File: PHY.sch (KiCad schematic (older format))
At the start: 70 parts

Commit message: Component placement
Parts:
- C10, C11, C12, C13, C14, C15, C16, C3, C4, C5, C6, C7, C8, C9: renamed from C?; footprint (none) -> Capacitor_SMD:C_0402_1005Metric
- D3: renamed from D?; footprint (none) -> LED_SMD:LED_0603_1608Metric
- J10: renamed from J?; footprint (none) -> Connector_RJ:RJ45_Hanrun_HR911105A
- JP1: renamed from J?; footprint (none) -> Connector_PinHeader_2.54mm:PinHeader_1x02_P2.54mm_Vertical
- JP2, JP3, JP4, JP5, JP6: renamed from J?; footprint (none) -> Connector_PinHeader_2.54mm:PinHeader_1x03_P2.54mm_Vertical
- R10, R11, R12, R13, R14, R15, R16, R17, R18, R19, R20, R21, R22, R23, R24, R25, R26, R27, R28, R29, R30, R31, R32, R33, R34, R35, R36, R37, R38, R39, R40, R41, R42, R43, R44, R45, R46, R47, R48, R49, R50, R6, R7, R8, R9: renamed from R?; footprint (none) -> Resistor_SMD:R_0402_1005Metric
- T1: renamed from T?; footprint (none) -> ak:Transformer_Pulse_H1100NL
- gave numbers to parts that had none: 2

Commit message: Test...
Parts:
- added R98, R99: 0, Resistor_SMD:R_1206_3216Metric, symbol Device:R_Small
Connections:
- net GND: now also R98.1, R99.1
- net GNDPWR: now also R98.2, R99.2
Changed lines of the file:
@@
 Text Label 9050 5900 0    50   ~ 0
 AN0
+$Comp
+L power:GNDPWR #PWR078
+U 1 1 5FE14DAE
+P 9250 3300
+F 0 "#PWR078" H 9250 3100 50  0001 C CNN
+F 1 "GNDPWR" H 9254 3146 50  0001 C CNN
+F 2 "" H 9250 3250 50  0001 C CNN
+F 3 "" H 9250 3250 50  0001 C CNN
+	1    9250 3300
+	1    0    0    -1
+$EndComp
+$Comp
+L Device:R_Small R99
+U 1 1 5FE160E3
+P 9400 3200
+F 0 "R99" V 9204 3200 50  0000 C CNN
+F 1 "0" V 9295 3200 50  0000 C CNN
+F 2 "Resistor_SMD:R_1206_3216Metric" H 9400 3200 50  0001 C CNN
+F 3 "~" H 9400 3200 50  0001 C CNN
+	1    9400 3200
+	0    1    1    0
+$EndComp
+$Comp
+L power:GND #PWR?
+U 1 1 5FE166F9
+P 9550 3300
+AR Path="/5FE166F9" Ref="#PWR?"  Part="1"
+AR Path="/6062FABA/5FE166F9" Ref="#PWR080"  Part="1"
+F 0 "#PWR080" H 9550 3050 50  0001 C CNN
+F 1 "GND" H 9555 3127 50  0001 C CNN
+F 2 "" H 9550 3300 50  0001 C CNN
+F 3 "" H 9550 3300 50  0001 C CNN
+	1    9550 3300
+	-1   0    0    -1
+$EndComp
+Wire Wire Line
+	9550 3300 9550 3200
+Wire Wire Line
+	9550 3200 9500 3200
+Wire Wire Line
+	9250 3300 9250 3200
+Wire Wire Line
+	9250 3200 9300 3200
+$Comp
+L power:GNDPWR #PWR077
+U 1 1 5FEADB75
+P 9250 1500
+F 0 "#PWR077" H 9250 1300 50  0001 C CNN
+F 1 "GNDPWR" H 9254 1346 50  0001 C CNN
+F 2 "" H 9250 1450 50  0001 C CNN
+F 3 "" H 9250 1450 50  0001 C CNN
+	1    9250 1500
+	1    0    0    -1
+$EndComp
+$Comp
+L Device:R_Small R98
+U 1 1 5FEADB7B
+P 9400 1400
+F 0 "R98" V 9204 1400 50  0000 C CNN
+F 1 "0" V 9295 1400 50  0000 C CNN
+F 2 "Resistor_SMD:R_1206_3216Metric" H 9400 1400 50  0001 C CNN
+F 3 "~" H 9400 1400 50  0001 C CNN
+	1    9400 1400
+	0    1    1    0
+$EndComp
+$Comp
+L power:GND #PWR?
+U 1 1 5FEADB81
+P 9550 1500
+AR Path="/5FEADB81" Ref="#PWR?"  Part="1"
+AR Path="/6062FABA/5FEADB81" Ref="#PWR079"  Part="1"
+F 0 "#PWR079" H 9550 1250 50  0001 C CNN
+F 1 "GND" H 9555 1327 50  0001 C CNN
+F 2 "" H 9550 1500 50  0001 C CNN
+F 3 "" H 9550 1500 50  0001 C CNN
+	1    9550 1500
+	-1   0    0    -1
+$EndComp
+Wire Wire Line
+	9550 1500 9550 1400
+Wire Wire Line
+	9550 1400 9500 1400
+Wire Wire Line
+	9250 1500 9250 1400
+Wire Wire Line
+	9250 1400 9300 1400
 $EndSCHEMATC

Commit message: Placement
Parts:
- removed R30, R31: 0, Resistor_SMD:R_0402_1005Metric, symbol Device:R_Small
- C10, C4: footprint Capacitor_SMD:C_0402_1005Metric -> Capacitor_Tantalum_SMD:CP_EIA-3216-18_Kemet-A; LCSC (none) -> C7171
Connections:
- net +3V3: now also C11.1, C12.1, R25.2, R26.1, R27.2, R28.1
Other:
- moved on the sheet: R38, R39, R40, R41
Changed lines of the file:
@@
 Wire Wire Line
 	6000 2700 6000 2750
-$Comp
-L Device:R_Small R?
-U 1 1 607C1FFB
-P 6000 2600
-AR Path="/607C1FFB" Ref="R?"  Part="1"
-AR Path="/6062FABA/607C1FFB" Ref="R31"  Part="1"
-F 0 "R31" H 5941 2646 50  0000 R CNN
-F 1 "0" H 5941 2555 50  0000 R CNN
-F 2 "Resistor_SMD:R_0402_1005Metric" H 6000 2600 50  0001 C CNN
-F 3 "~" H 6000 2600 50  0001 C CNN
-	1    6000 2600
-	-1   0    0    -1
-$EndComp
-$Comp
-L Device:R_Small R?
-U 1 1 607AB601
-P 6000 1550
-AR Path="/607AB601" Ref="R?"  Part="1"
-AR Path="/6062FABA/607AB601" Ref="R30"  Part="1"
-F 0 "R30" H 5941 1596 50  0000 R CNN
-F 1 "0" H 5941 1505 50  0000 R CNN
-F 2 "Resistor_SMD:R_0402_1005Metric" H 6000 1550 50  0001 C CNN
-F 3 "~" H 6000 1550 50  0001 C CNN
-	1    6000 1550
-	-1   0    0    -1
-$EndComp
 Wire Wire Line
 	5450 1900 4850 1900
@@
 	8250 2400 8000 2400
 Wire Wire Line
-	8250 2400 8250 2900
+	8250 2400 8250 2850
 Wire Wire Line
 	9050 2250 8000 2250
@@
 Connection ~ 8450 3200
 Wire Wire Line
-	8250 3200 8250 3100
+	8250 3200 8250 3050
 Wire Wire Line
 	8450 3200 8250 3200
 Connection ~ 8650 3200
 Wire Wire Line
-	8450 3200 8450 3100
+	8450 3200 8450 3050
 Wire Wire Line
 	8650 3200 8550 3200
 Wire Wire Line
-	8650 3200 8650 3100
+	8650 3200 8650 3050
 Wire Wire Line
 	8850 3200 8650 3200
 Wire Wire Line
-	8850 3100 8850 3200
+	8850 3050 8850 3200
 Wire Wire Line
 	9000 2400 9000 2450
 Connection ~ 9000 2400
 Wire Wire Line
-	8650 2400 8650 2900
+	8650 2400 8650 2850
 Wire Wire Line
 	9000 2400 8650 2400
@@
 Connection ~ 9000 2700
 Wire Wire Line
-	8850 2700 8850 2900
+	8850 2700 8850 2850
 Wire Wire Line
 	9000 2700 8850 2700
@@
 L Device:R_Small R?
 U 1 1 6065AB7F
-P 8850 3000
+P 8850 2950
 AR Path="/6065AB7F" Ref="R?"  Part="1"
 AR Path="/6062FABA/6065AB7F" Ref="R41"  Part="1"
-F 0 "R41" H 8791 3046 50  0000 R CNN
-F 1 "75" H 8791 2955 50  0000 R CNN
-F 2 "Resistor_SMD:R_0402_1005Metric" H 8850 3000 50  0001 C CNN
-F 3 "~" H 8850 3000 50  0001 C CNN
-	1    8850 3000
+F 0 "R41" V 8900 3200 50  0000 R CNN
+F 1 "75" V 8900 2850 50  0000 R CNN
+F 2 "Resistor_SMD:R_0402_1005Metric" H 8850 2950 50  0001 C CNN
+F 3 "~" H 8850 2950 50  0001 C CNN
+	1    8850 2950
 	-1   0    0    -1
 $EndComp
@@
 L Device:R_Small R?
 U 1 1 6065AB85
-P 8650 3000
+P 8650 2950
 AR Path="/6065AB85" Ref="R?"  Part="1"
 AR Path="/6062FABA/6065AB85" Ref="R40"  Part="1"
-F 0 "R40" H 8591 3046 50  0000 R CNN
-F 1 "75" H 8591 2955 50  0000 R CNN
-F 2 "Resistor_SMD:R_0402_1005Metric" H 8650 3000 50  0001 C CNN
-F 3 "~" H 8650 3000 50  0001 C CNN
-	1    8650 3000
+F 0 "R40" V 8700 3200 50  0000 R CNN
+F 1 "75" V 8700 2850 50  0000 R CNN
+F 2 "Resistor_SMD:R_0402_1005Metric" H 8650 2950 50  0001 C CNN
+F 3 "~" H 8650 2950 50  0001 C CNN
+	1    8650 2950
 	-1   0    0    -1
 $EndComp
@@
 L Device:R_Small R?
 U 1 1 6065AB8D
-P 8450 3000
+P 8450 2950
 AR Path="/6065AB8D" Ref="R?"  Part="1"
 AR Path="/6062FABA/6065AB8D" Ref="R39"  Part="1"
-F 0 "R39" H 8391 3046 50  0000 R CNN
-F 1 "75" H 8391 2955 50  0000 R CNN
-F 2 "Resistor_SMD:R_0402_1005Metric" H 8450 3000 50  0001 C CNN
-F 3 "~" H 8450 3000 50  0001 C CNN
-	1    8450 3000
+F 0 "R39" V 8500 3200 50  0000 R CNN
+F 1 "75" V 8500 2850 50  0000 R CNN
+F 2 "Resistor_SMD:R_0402_1005Metric" H 8450 2950 50  0001 C CNN
+F 3 "~" H 8450 2950 50  0001 C CNN
+	1    8450 2950
 	-1   0    0    -1
 $EndComp
@@
 L Device:R_Small R?
 U 1 1 6065AB93
-P 8250 3000
+P 8250 2950
 AR Path="/6065AB93" Ref="R?"  Part="1"
 AR Path="/6062FABA/6065AB93" Ref="R38"  Part="1"
-F 0 "R38" H 8191 3046 50  0000 R CNN
-F 1 "75" H 8191 2955 50  0000 R CNN
-F 2 "Resistor_SMD:R_0402_1005Metric" H 8250 3000 50  0001 C CNN
-F 3 "~" H 8250 3000 50  0001 C CNN
-	1    8250 3000
+F 0 "R38" V 8300 3200 50  0000 R CNN
+F 1 "75" V 8300 2850 50  0000 R CNN
+F 2 "Resistor_SMD:R_0402_1005Metric" H 8250 2950 50  0001 C CNN
+F 3 "~" H 8250 2950 50  0001 C CNN
+	1    8250 2950
 	-1   0    0    -1
 $EndComp
@@
 	8650 1850 8000 1850
 Wire Wire Line
-	8450 2900 8450 1700
+	8450 2850 8450 1700
 Wire Wire Line
 	8450 1700 8000 1700
@@
 L power:+3V3 #PWR?
 U 1 1 606A9712
-P 6000 2500
+P 6000 2700
 AR Path="/606A9712" Ref="#PWR?"  Part="1"
 AR Path="/6062FABA/606A9712" Ref="#PWR038"  Part="1"
-F 0 "#PWR038" H 6000 2350 50  0001 C CNN
-F 1 "+3V3" H 6015 2673 50  0000 C CNN
-F 2 "" H 6000 2500 50  0001 C CNN
-F 3 "" H 6000 2500 50  0001 C CNN
-	1    6000 2500
+F 0 "#PWR038" H 6000 2550 50  0001 C CNN
+F 1 "+3V3" H 6015 2873 50  0000 C CNN
+F 2 "" H 6000 2700 50  0001 C CNN
+F 3 "" H 6000 2700 50  0001 C CNN
+	1    6000 2700
 	-1   0    0    -1
 $EndComp
@@
 L power:+3V3 #PWR?
 U 1 1 60693425
-P 6000 1450
+P 6000 1650
 AR Path="/60693425" Ref="#PWR?"  Part="1"
 AR Path="/6062FABA/60693425" Ref="#PWR036"  Part="1"
-F 0 "#PWR036" H 6000 1300 50  0001 C CNN
-F 1 "+3V3" H 6015 1623 50  0000 C CNN
-F 2 "" H 6000 1450 50  0001 C CNN
-F 3 "" H 6000 1450 50  0001 C CNN
-	1    6000 1450
+F 0 "#PWR036" H 6000 1500 50  0001 C CNN
+F 1 "+3V3" H 6015 1823 50  0000 C CNN
+F 2 "" H 6000 1650 50  0001 C CNN
+F 3 "" H 6000 1650 50  0001 C CNN
+	1    6000 1650
 	-1   0    0    -1
 $EndComp
@@
 F 0 "C10" H 5758 4696 50  0000 R CNN
 F 1 "10uF" H 5758 4605 50  0000 R CNN
-F 2 "Capacitor_SMD:C_0402_1005Metric" H 5850 4650 50  0001 C CNN
+F 2 "Capacitor_Tantalum_SMD:CP_EIA-3216-18_Kemet-A" H 5850 4650 50  0001 C CNN
 F 3 "~" H 5850 4650 50  0001 C CNN
+F 4 "C7171" H 5850 4650 50  0001 C CNN "LCSC"
 	1    5850 4650
 	-1   0    0    -1
@@
 F 0 "C4" H 3008 1046 50  0000 R CNN
 F 1 "10uF" H 3008 955 50  0000 R CNN
-F 2 "Capacitor_SMD:C_0402_1005Metric" H 3100 1000 50  0001 C CNN
+F 2 "Capacitor_Tantalum_SMD:CP_EIA-3216-18_Kemet-A" H 3100 1000 50  0001 C CNN
 F 3 "~" H 3100 1000 50  0001 C CNN
+F 4 "C7171" H 3100 1000 50  0001 C CNN "LCSC"
 	1    3100 1000
 	-1   0    0    -1

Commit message: Routing
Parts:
- C10, C4: symbol Device:C_Small -> Device:CP_Small
- J10: footprint Connector_RJ:RJ45_Hanrun_HR911105A -> Connector_RJ:RJ45_Amphenol_RJHSE538X
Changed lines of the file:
@@
 F 0 "J10" H 9250 1900 50  0000 C CNN
 F 1 "RJ45_LED_Shielded" H 9400 2900 50  0000 C CNN
-F 2 "Connector_RJ:RJ45_Hanrun_HR911105A" V 9450 2375 50  0001 C CNN
+F 2 "Connector_RJ:RJ45_Amphenol_RJHSE538X" V 9450 2375 50  0001 C CNN
 F 3 "~" V 9450 2375 50  0001 C CNN
 	1    9450 2350
@@
 	5850 4200 5850 4550
 $Comp
-L Device:C_Small C?
+L Device:CP_Small C?
 U 1 1 60AA936A
 P 5850 4650
@@
 	3100 900  3100 850
 $Comp
-L Device:C_Small C?
+L Device:CP_Small C?
 U 1 1 60B06127
 P 3100 1000

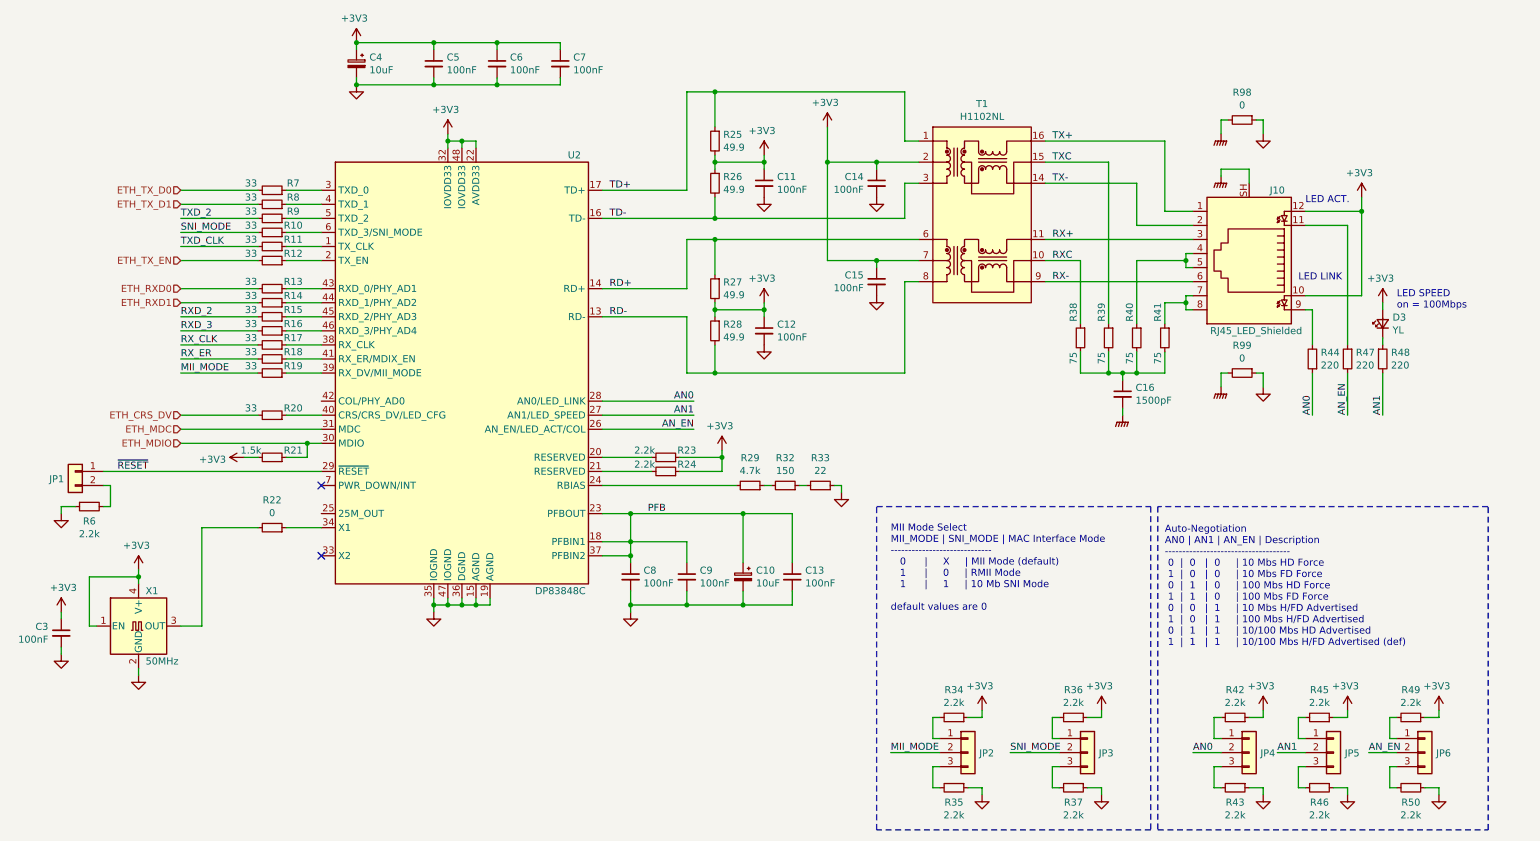
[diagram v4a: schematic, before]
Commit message: Added ESD protection
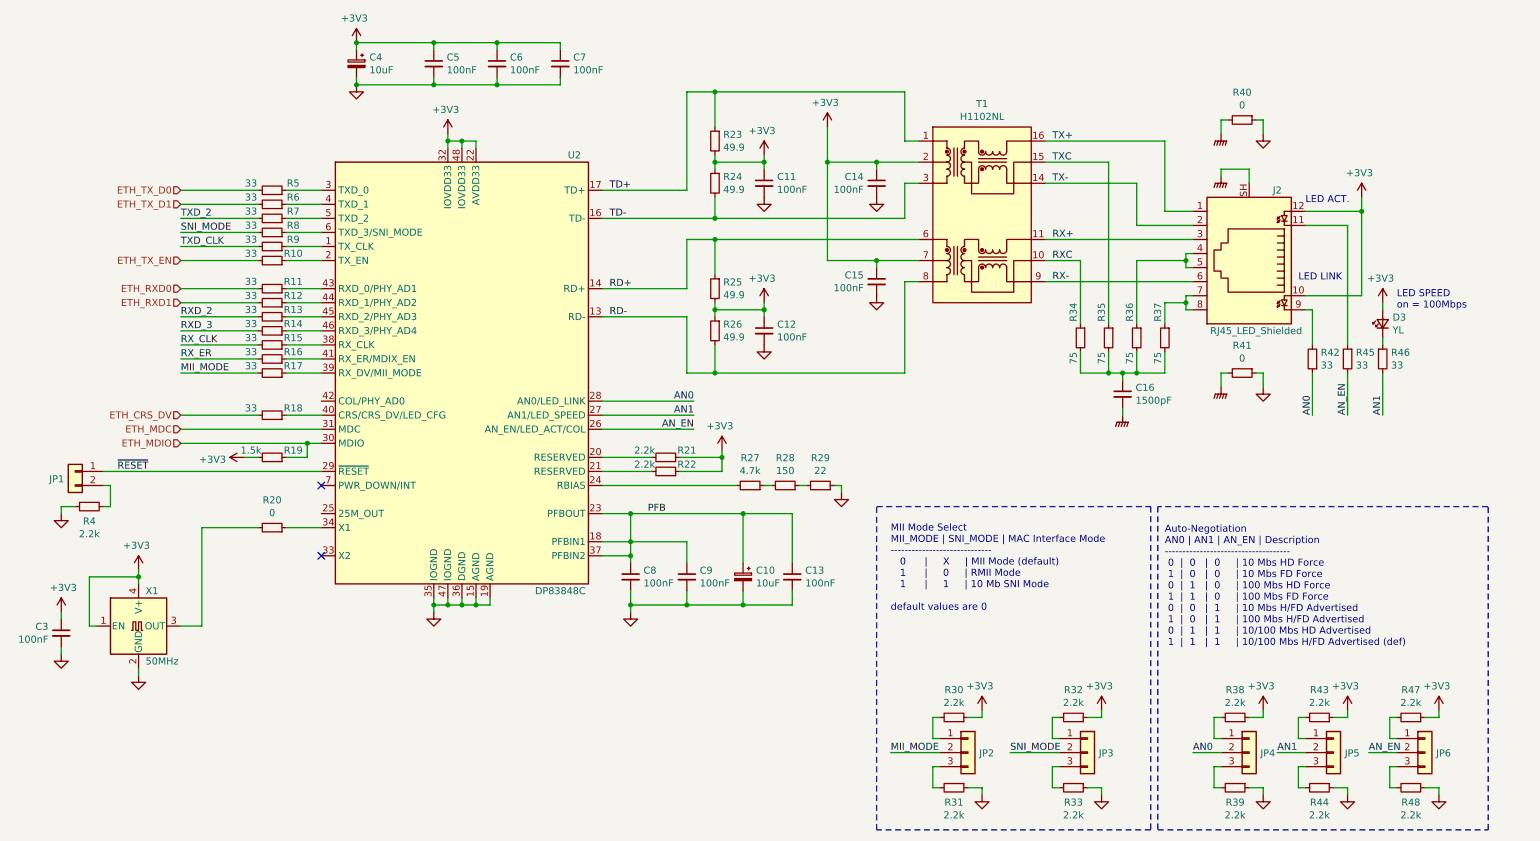
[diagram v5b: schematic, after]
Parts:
- R42: renamed from R44; value 220 -> 33
- R45: renamed from R47; value 220 -> 33
- R46: renamed from R48; value 220 -> 33
- renumbered J10 to J2, R12 to R10, R13 to R11, R14 to R12, R15 to R13, R16 to R14, R17 to R15, R18 to R16, R19 to R17, R20 to R18, R21 to R19, R22 to R20, R23 to R21, R24 to R22, R25 to R23, R26 to R24, R27 to R25, R28 to R26, R29 to R27, R32 to R28, R33 to R29, R34 to R30, R35 to R31, R36 to R32, R37 to R33, R38 to R34, R39 to R35, R40 to R36, R41 to R37, R42 to R38, R43 to R39, R6 to R4, R98 to R40, R99 to R41, R45 to R43, R46 to R44, R49 to R47, R50 to R48, R7 to R5, R8 to R6, R9 to R7, R10 to R8, R11 to R9

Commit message: Layout
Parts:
- removed R16, R7, R9: 33, Resistor_SMD:R_0402_1005Metric, symbol Device:R_Small
- R19: value 1.5k -> 2.2k
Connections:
- net RXD_2 is gone; now on net ETH_MDC: R13.2
- net RXD_3 is gone; now on net ETH_MDIO: R14.2
- net ETH_MDC: no longer U2.31 (MDC)
- net ETH_MDIO: no longer R19.1, U2.30 (MDIO)
- net at R13.1: now also U2.31 (MDC); no longer U2.45 (RXD_2/PHY_AD3)
- net at R14.1: now also R19.1, U2.30 (MDIO); no longer U2.46 (RXD_3/PHY_AD4)
- no-connect marks 2 -> 9
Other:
- moved on the sheet: C3, JP1, R19, R4, X1

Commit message: Layout
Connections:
- net GNDPWR renamed Earth
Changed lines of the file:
@@
 	9050 2250 8000 2250
-Wire Wire Line
-	9050 2550 8000 2550
 Wire Wire Line
 	8850 2050 9050 2050
@@
 Text Label 8050 2400 0    50   ~ 0
 RXC
-Text Label 8050 2550 0    50   ~ 0
-RX-
 Wire Wire Line
 	8550 3500 8550 3450
@@
 	1    5650 1550
 	-1   0    0    -1
-$EndComp
-$Comp
-L ak:H1102NL T?
-U 1 1 6065AB5E
-P 7300 1550
-AR Path="/6065AB5E" Ref="T?"  Part="1"
-AR Path="/6062FABA/6065AB5E" Ref="T1"  Part="1"
-F 0 "T1" H 7550 1815 50  0000 C CNN
-F 1 "H1102NL" H 7550 1724 50  0000 C CNN
-F 2 "ak:Transformer_Pulse_H1100NL" H 7225 1700 50  0001 C CNN
-F 3 "" H 7225 1700 50  0001 C CNN
-	1    7300 1550
-	1    0    0    -1
 $EndComp
 $Comp
@@
 	5700 3750 5700 3800
 Connection ~ 5700 3800
-$Comp
-L power:GNDPWR #PWR037
-U 1 1 60B048E5
-P 8550 3500
-F 0 "#PWR037" H 8550 3300 50  0001 C CNN
-F 1 "GNDPWR" H 8554 3346 50  0001 C CNN
-F 2 "" H 8550 3450 50  0001 C CNN
-F 3 "" H 8550 3450 50  0001 C CNN
-	1    8550 3500
-	1    0    0    -1
-$EndComp
-$Comp
-L power:GNDPWR #PWR039
-U 1 1 60B05B06
-P 9250 1800
-F 0 "#PWR039" H 9250 1600 50  0001 C CNN
-F 1 "GNDPWR" H 9254 1646 50  0001 C CNN
-F 2 "" H 9250 1750 50  0001 C CNN
-F 3 "" H 9250 1750 50  0001 C CNN
-	1    9250 1800
-	1    0    0    -1
-$EndComp
 Wire Wire Line
 	1850 3700 2400 3700
@@
 AN0
 $Comp
-L power:GNDPWR #PWR040
-U 1 1 5FE14DAE
-P 9250 3300
-F 0 "#PWR040" H 9250 3100 50  0001 C CNN
-F 1 "GNDPWR" H 9254 3146 50  0001 C CNN
-F 2 "" H 9250 3250 50  0001 C CNN
-F 3 "" H 9250 3250 50  0001 C CNN
-	1    9250 3300
-	1    0    0    -1
-$EndComp
-$Comp
 L Device:R_Small R41
 U 1 1 5FE160E3
@@
 	9250 3200 9300 3200
 $Comp
-L power:GNDPWR #PWR038
-U 1 1 5FEADB75
-P 9250 1500
-F 0 "#PWR038" H 9250 1300 50  0001 C CNN
-F 1 "GNDPWR" H 9254 1346 50  0001 C CNN
-F 2 "" H 9250 1450 50  0001 C CNN
-F 3 "" H 9250 1450 50  0001 C CNN
-	1    9250 1500
-	1    0    0    -1
-$EndComp
-$Comp
 L Device:R_Small R40
 U 1 1 5FEADB7B
@@
 NoConn ~ 2850 2100
 NoConn ~ 2850 2300
+$Comp
+L ak:H1102NL T?
+U 1 1 6065AB5E
+P 7300 1550
+AR Path="/6065AB5E" Ref="T?"  Part="1"
+AR Path="/6062FABA/6065AB5E" Ref="T1"  Part="1"
+F 0 "T1" H 7550 1815 50  0000 C CNN
+F 1 "H1102NL" H 7550 1724 50  0000 C CNN
+F 2 "ak:Transformer_Pulse_H1100NL" H 7225 1700 50  0001 C CNN
+F 3 "" H 7225 1700 50  0001 C CNN
+	1    7300 1550
+	1    0    0    -1
+$EndComp
+Text Label 8050 2550 0    50   ~ 0
+RX-
+Wire Wire Line
+	9050 2550 8000 2550
+$Comp
+L power:Earth #PWR0111
+U 1 1 5FFB97C0
+P 9250 3300
+F 0 "#PWR0111" H 9250 3050 50  0001 C CNN
+F 1 "Earth" H 9250 3150 50  0001 C CNN
+F 2 "" H 9250 3300 50  0001 C CNN
+F 3 "~" H 9250 3300 50  0001 C CNN
+	1    9250 3300
+	1    0    0    -1
+$EndComp
+$Comp
+L power:Earth #PWR0112
+U 1 1 5FFCDEDE
+P 8550 3500
+F 0 "#PWR0112" H 8550 3250 50  0001 C CNN
+F 1 "Earth" H 8550 3350 50  0001 C CNN
+F 2 "" H 8550 3500 50  0001 C CNN
+F 3 "~" H 8550 3500 50  0001 C CNN
+	1    8550 3500
+	1    0    0    -1
+$EndComp
+$Comp
+L power:Earth #PWR?
+U 1 1 5FFD1A34
+P 9250 1800
+F 0 "#PWR?" H 9250 1550 50  0001 C CNN
+F 1 "Earth" H 9250 1650 50  0001 C CNN
+F 2 "" H 9250 1800 50  0001 C CNN
+F 3 "~" H 9250 1800 50  0001 C CNN
+	1    9250 1800
+	1    0    0    -1
+$EndComp
+$Comp
+L power:Earth #PWR?
+U 1 1 5FFD1E16
+P 9250 1500
+F 0 "#PWR?" H 9250 1250 50  0001 C CNN
+F 1 "Earth" H 9250 1350 50  0001 C CNN
+F 2 "" H 9250 1500 50  0001 C CNN
+F 3 "~" H 9250 1500 50  0001 C CNN
+	1    9250 1500
+	1    0    0    -1
+$EndComp
 $EndSCHEMATC
